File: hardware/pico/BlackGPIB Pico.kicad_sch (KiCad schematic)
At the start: 20 parts, among them J3 Micro_SD_Card, U1 SN75160, U2 SN75160, U3 SN75161, U4 SN75161, U5 SN75162, U6 SN75162

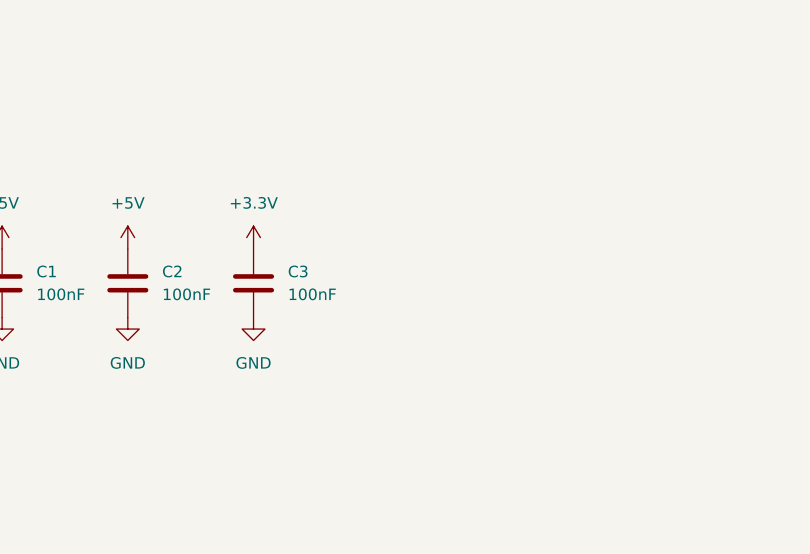
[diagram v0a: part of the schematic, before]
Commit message: pico: add 47uF tantalum capacitor near sd card slot to rev 1 board
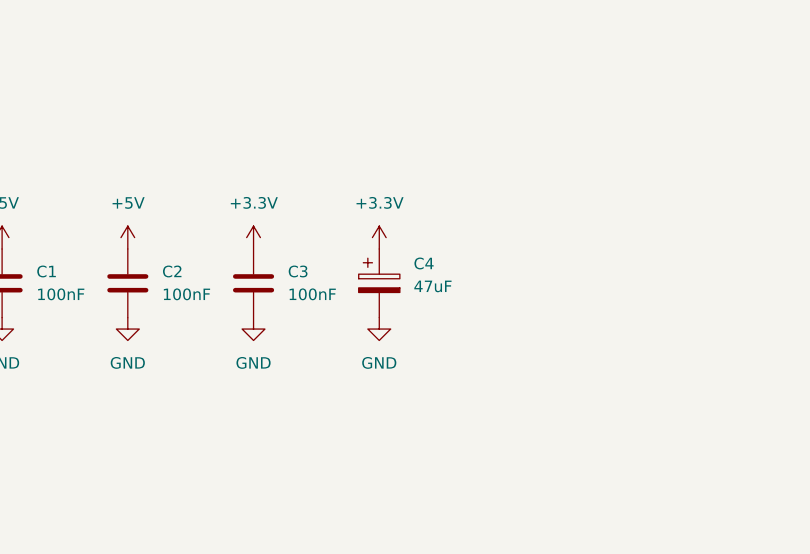
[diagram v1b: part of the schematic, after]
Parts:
- added C4: 47uF, Capacitor_Tantalum_SMD:CP_EIA-6032-15_Kemet-U_HandSolder, symbol Device:C_Polarized
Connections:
- net +3.3V: now also C4.1
- net GND: now also C4.2
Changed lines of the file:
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@@
+	(symbol
+		(lib_id "power:GND")
+		(at 105.41 322.58 0)
+		(unit 1)
+		(exclude_from_sim no)
+		(in_bom yes)
+		(on_board yes)
+		(dnp no)
+		(fields_autoplaced yes)
+		(property "Reference" "#PWR035"
+			(at 105.41 328.93 0)
+			(effects
+				(font
+					(size 1.27 1.27)
+				)
+				(hide yes)
+			)
+		)
+		(property "Value" "GND"
+			(at 105.41 327.66 0)
+			(effects
+				(font
+					(size 1.27 1.27)
+				)
+			)
+		)
+		(property "Footprint" ""
+			(at 105.41 322.58 0)
+			(effects
+				(font
+					(size 1.27 1.27)
+				)
+				(hide yes)
+			)
+		)
+		(property "Datasheet" ""
+			(at 105.41 322.58 0)
+			(effects
+				(font
+					(size 1.27 1.27)
+				)
+				(hide yes)
+			)
+		)
+		(property "Description" "Power symbol creates a global label with name \"GND\" , ground"
+			(at 105.41 322.58 0)
+			(effects
+				(font
+					(size 1.27 1.27)
+				)
+				(hide yes)
+			)
+		)
+		(pin "1"
+		)
+		(instances
+			(project "BlackGPIB Pico"
+				(path "/deebe9f4-cb8a-4d56-8826-fc9325a93a72"
+					(reference "#PWR035")
+					(unit 1)
+				)
+			)
+		)
+	)
 	(symbol
 		(lib_id "power:GND")
@@
 	)
 	(symbol
+		(lib_id "power:+3.3V")
+		(at 105.41 314.96 0)
+		(unit 1)
+		(exclude_from_sim no)
+		(in_bom yes)
+		(on_board yes)
+		(dnp no)
+		(fields_autoplaced yes)
+		(property "Reference" "#PWR034"
+			(at 105.41 318.77 0)
+			(effects
+				(font
+					(size 1.27 1.27)
+				)
+				(hide yes)
+			)
+		)
+		(property "Value" "+3.3V"
+			(at 105.41 309.88 0)
+			(effects
+				(font
+					(size 1.27 1.27)
+				)
+			)
+		)
+		(property "Footprint" ""
+			(at 105.41 314.96 0)
+			(effects
+				(font
+					(size 1.27 1.27)
+				)
+				(hide yes)
+			)
+		)
+		(property "Datasheet" ""
+			(at 105.41 314.96 0)
+			(effects
+				(font
+					(size 1.27 1.27)
+				)
+				(hide yes)
+			)
+		)
+		(property "Description" "Power symbol creates a global label with name \"+3.3V\""
+			(at 105.41 314.96 0)
+			(effects
+				(font
+					(size 1.27 1.27)
+				)
+				(hide yes)
+			)
+		)
+		(pin "1"
+		)
+		(instances
+			(project "BlackGPIB Pico"
+				(path "/deebe9f4-cb8a-4d56-8826-fc9325a93a72"
+					(reference "#PWR034")
+					(unit 1)
+				)
+			)
+		)
+	)
+	(symbol
 		(lib_id "BlackGPIB Pico:SN75161")
 		(at 220.98 317.5 0)
@@
 					(unit 1)
 				)
+			)
+		)
+	)
+	(symbol
+		(lib_id "Device:C_Polarized")
+		(at 105.41 318.77 0)
+		(unit 1)
+		(exclude_from_sim no)
+		(in_bom yes)
+		(on_board yes)
+		(dnp no)
+		(fields_autoplaced yes)
+		(property "Reference" "C4"
+			(at 109.22 316.6109 0)
+			(effects
+				(font
+					(size 1.27 1.27)
+				)
+				(justify left)
+			)
+		)
+		(property "Value" "47uF"
+			(at 109.22 319.1509 0)
+			(effects
+				(font
+					(size 1.27 1.27)
+				)
+				(justify left)
+			)
+		)
+		(property "Footprint" "Capacitor_Tantalum_SMD:CP_EIA-6032-15_Kemet-U_HandSolder"
+			(at 106.3752 322.58 0)
+			(effects
+				(font
+					(size 1.27 1.27)
+				)
+				(hide yes)
+			)
+		)
+		(property "Datasheet" "~"
+			(at 105.41 318.77 0)
+			(effects
+				(font
+					(size 1.27 1.27)
+				)
+				(hide yes)
+			)
+		)
+		(property "Description" "Polarized capacitor"
+			(at 105.41 318.77 0)
+			(effects
+				(font
+					(size 1.27 1.27)
+				)
+				(hide yes)
+			)
+		)
+		(pin "1"
+		)
+		(pin "2"
+		)
+		(instances
+			(project ""
+				(path "/deebe9f4-cb8a-4d56-8826-fc9325a93a72"
+					(reference "C4")
+					(unit 1)
+				)
